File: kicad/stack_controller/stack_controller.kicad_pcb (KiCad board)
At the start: 2 copper layers, 206.2 x 157 mm, 53 parts

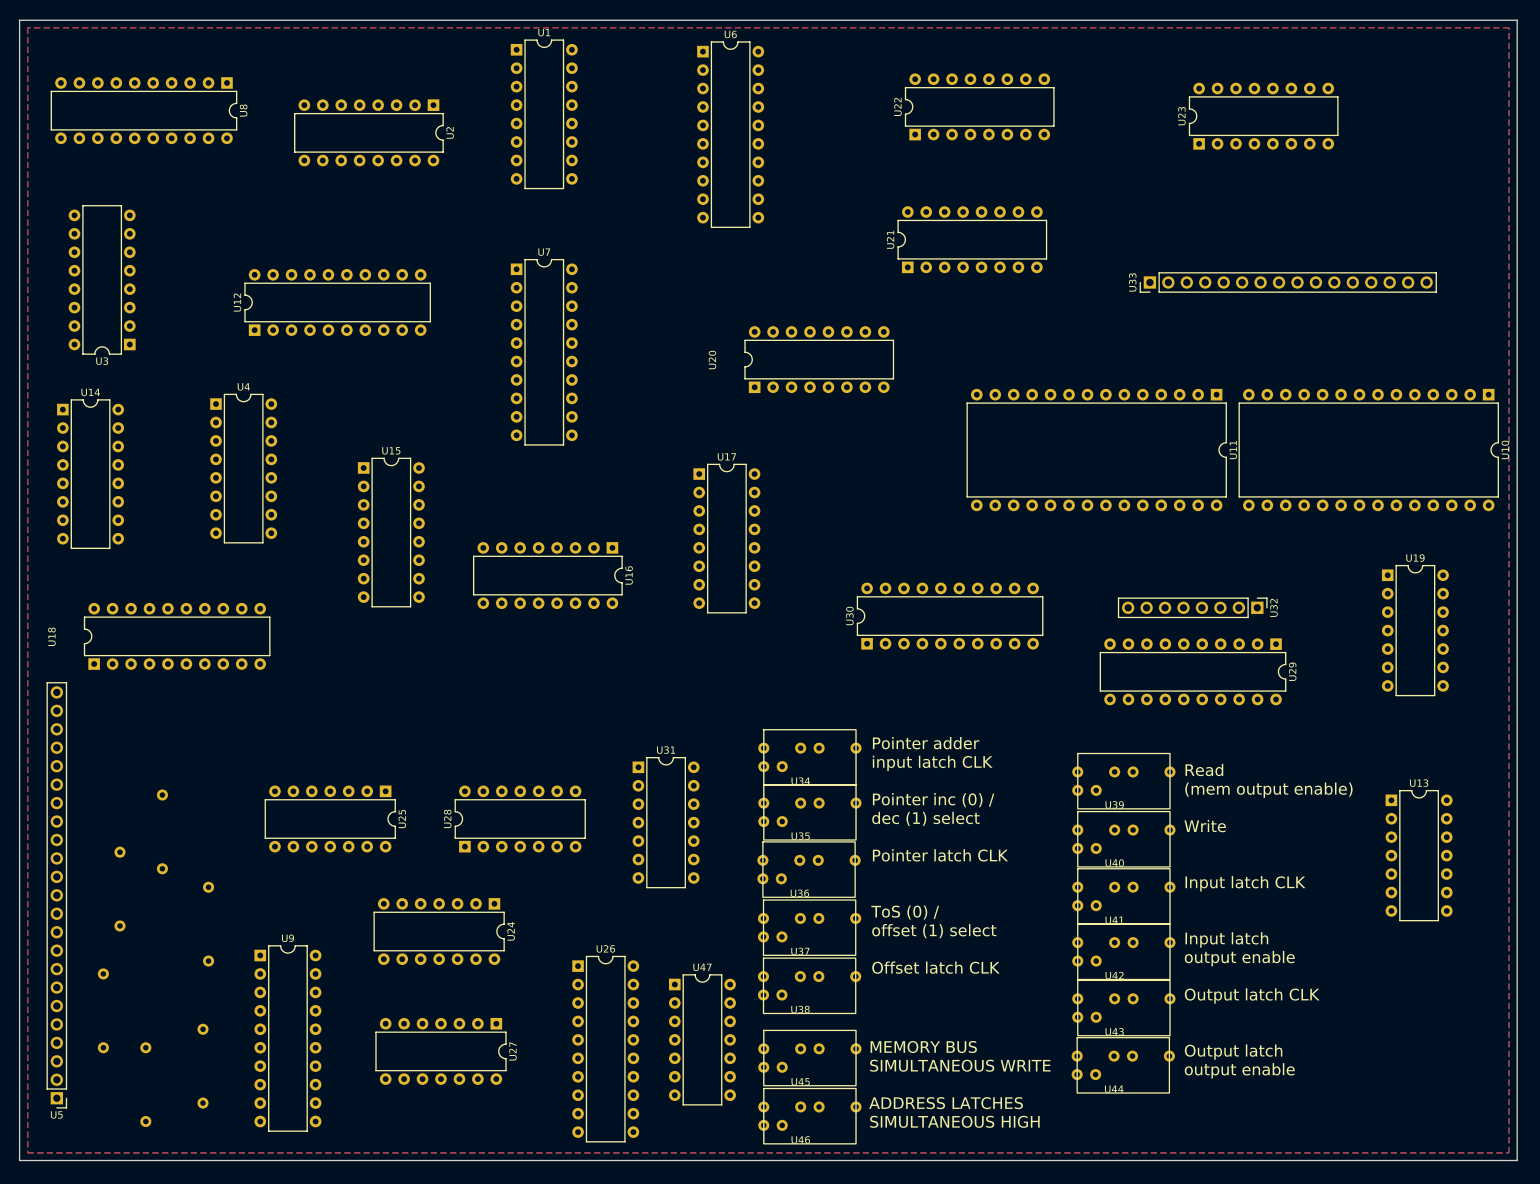
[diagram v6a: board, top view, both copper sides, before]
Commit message: Finished IO controller schematic
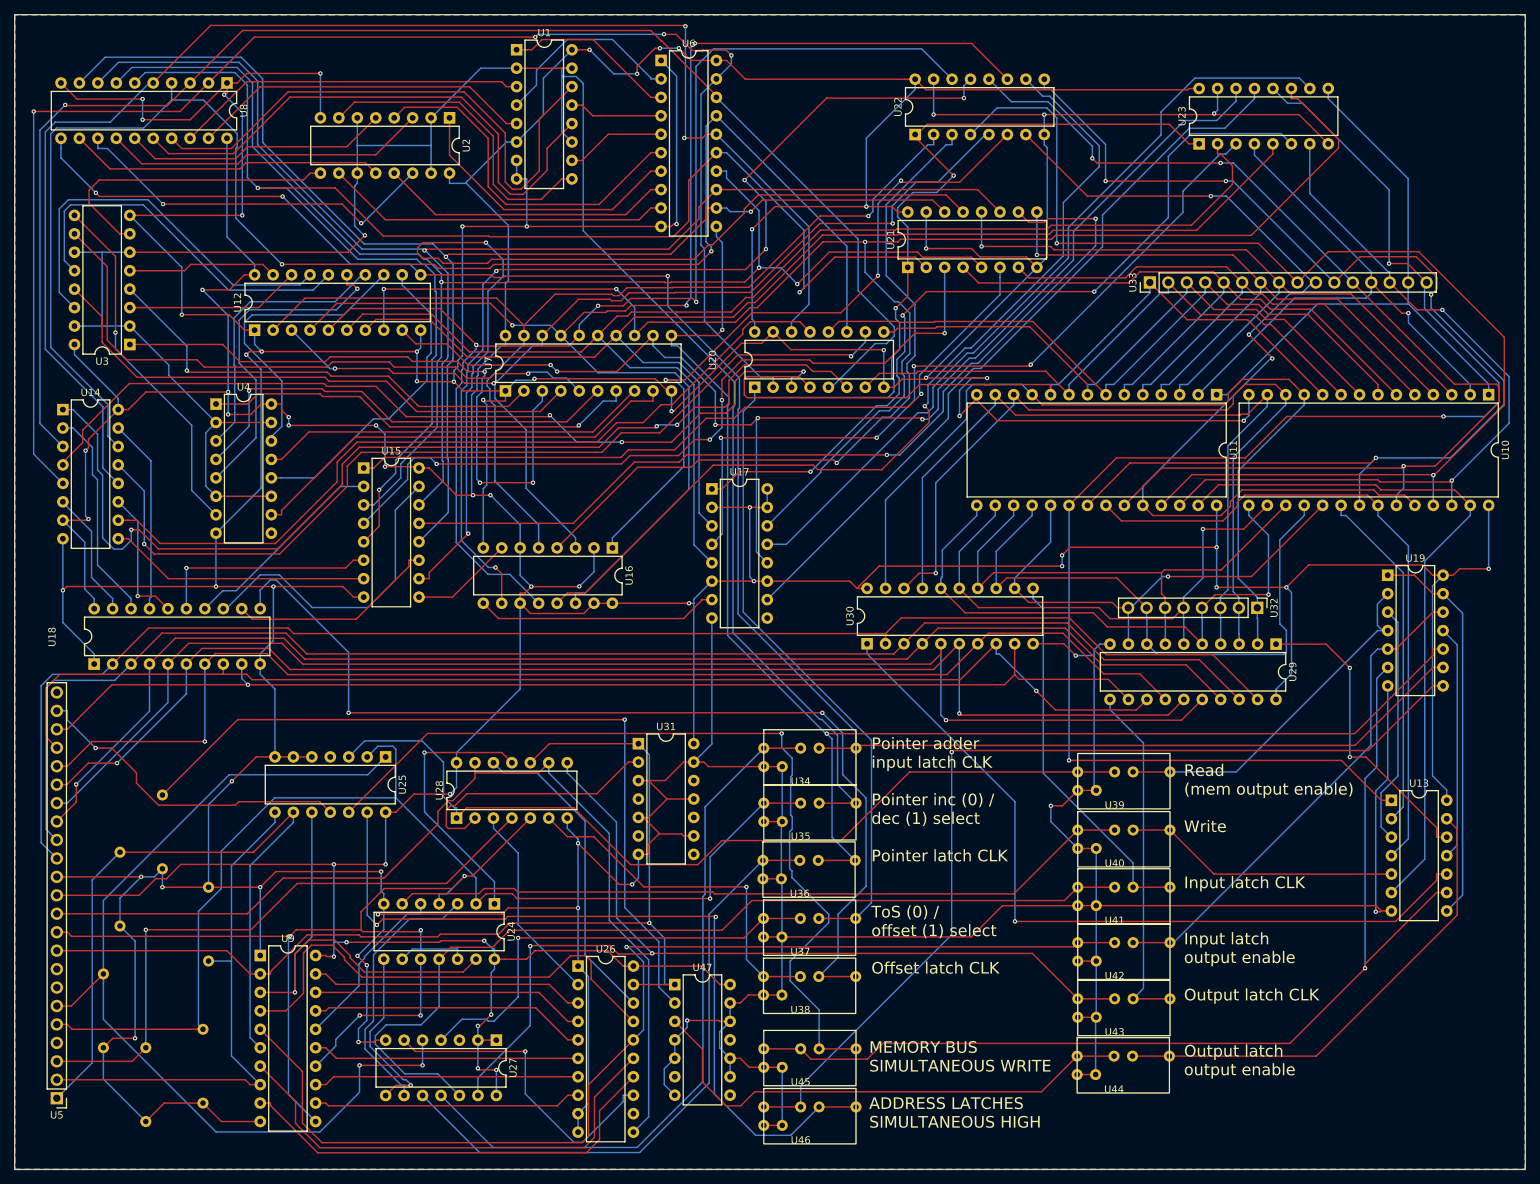
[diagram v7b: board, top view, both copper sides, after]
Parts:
- moved U7 16.8 mm to (100.6, 67.8), turned to 90 degrees
- moved U6 5.90 mm to (122.0, 22.3)
- moved U25 4.74 mm to (84.1, 118.2)
- moved U28 4.10 mm to (93.8, 126.6)
- moved U31 3.25 mm to (118.9, 116.4)
- moved U2 2.82 mm to (92.9, 30.2)
- moved U17 2.69 mm to (129.0, 81.3)
- moved U27 2.26 mm to (99.3, 157.2)
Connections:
- U14 pad 7: Net-(U1-C_IN) -> Net-(U1-B0)
- U5 pad 23: Net-(U47-1B) -> unconnected-(U5-ENABLE-Pad23)
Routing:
- net Net-(U1-C_IN): track 0.00 -> 1286.2 mm, vias 0 -> 46
- net Net-(U1-B0): track 0.00 -> 859.1 mm, vias 0 -> 38
- net Net-(U1-B1): track 0.00 -> 296.0 mm, vias 0 -> 1
- net Net-(U12-CLK): track 0.00 -> 259.6 mm, vias 0 -> 3
- net Net-(U15-A0): track 0.00 -> 221.2 mm, vias 0 -> 3
- net Net-(U14-A2): track 0.00 -> 216.5 mm, vias 0 -> 2
- net Net-(U12-D6): track 0.00 -> 215.3 mm, vias 0 -> 3
- net Net-(U14-A0): track 0.00 -> 207.2 mm, vias 0 -> 4
- net Net-(U11-CE#): track 0.00 -> 205.9 mm, vias 0 -> 3
- net Net-(U18-D0): track 0.00 -> 202.7 mm
- net Net-(U14-A1): track 0.00 -> 202.7 mm, vias 0 -> 1
- net Net-(U19-4A): track 0.00 -> 200.6 mm, vias 0 -> 2
- net Net-(U14-A3): track 0.00 -> 200.4 mm, vias 0 -> 2
- net Net-(U18-D1): track 0.00 -> 196.2 mm
- net Net-(U12-D2): track 0.00 -> 196.2 mm, vias 0 -> 3
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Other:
- board size 206.2 x 157 mm -> 208 x 159 mm
